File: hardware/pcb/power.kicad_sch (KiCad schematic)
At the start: 49 parts, among them J1 LiPo, J12 Solar, J13 USB-C, U1 AP63205, U11 USBLC6, U12 TP5100, U7 CN3722, U8 MT3608

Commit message: fix(sch): update J1 and L2 footprints in power.kicad_sch
J1 was still referencing the old Connector_JST:JST_XH_B2B-XH-AM footprint
after the switch to XT30PW-F. L2 was still referencing L_2512_6332Metric
after the footprint correction to L_Vishay_IFSC-1515AH_4x4x1.8mm.
Both caused errors in KiCad netlist import.

Co-Authored-By: Claude Sonnet 4.6 <noreply@anthropic.com>
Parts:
- J1: footprint Connector_JST:JST_XH_B2B-XH-AM_1x02_P2.50mm_Horizontal -> WellD:XT30PW-F_RightAngle
- L2: footprint Inductor_SMD:L_2512_6332Metric -> Inductor_SMD:L_Vishay_IFSC-1515AH_4x4x1.8mm
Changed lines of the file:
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@@
 			)
 		)
-		(property "Footprint" "Connector_JST:JST_XH_B2B-XH-AM_1x02_P2.50mm_Horizontal"
+		(property "Footprint" "WellD:XT30PW-F_RightAngle"
 			(at 0 0 0)
 			(hide yes)
@@
 			)
 		)
-		(property "Footprint" "Inductor_SMD:L_2512_6332Metric"
-			(at 0 0 0)
-			(hide yes)
+		(property "Footprint" "Inductor_SMD:L_Vishay_IFSC-1515AH_4x4x1.8mm"
+			(at 0 0 0)
+			(hide yes)

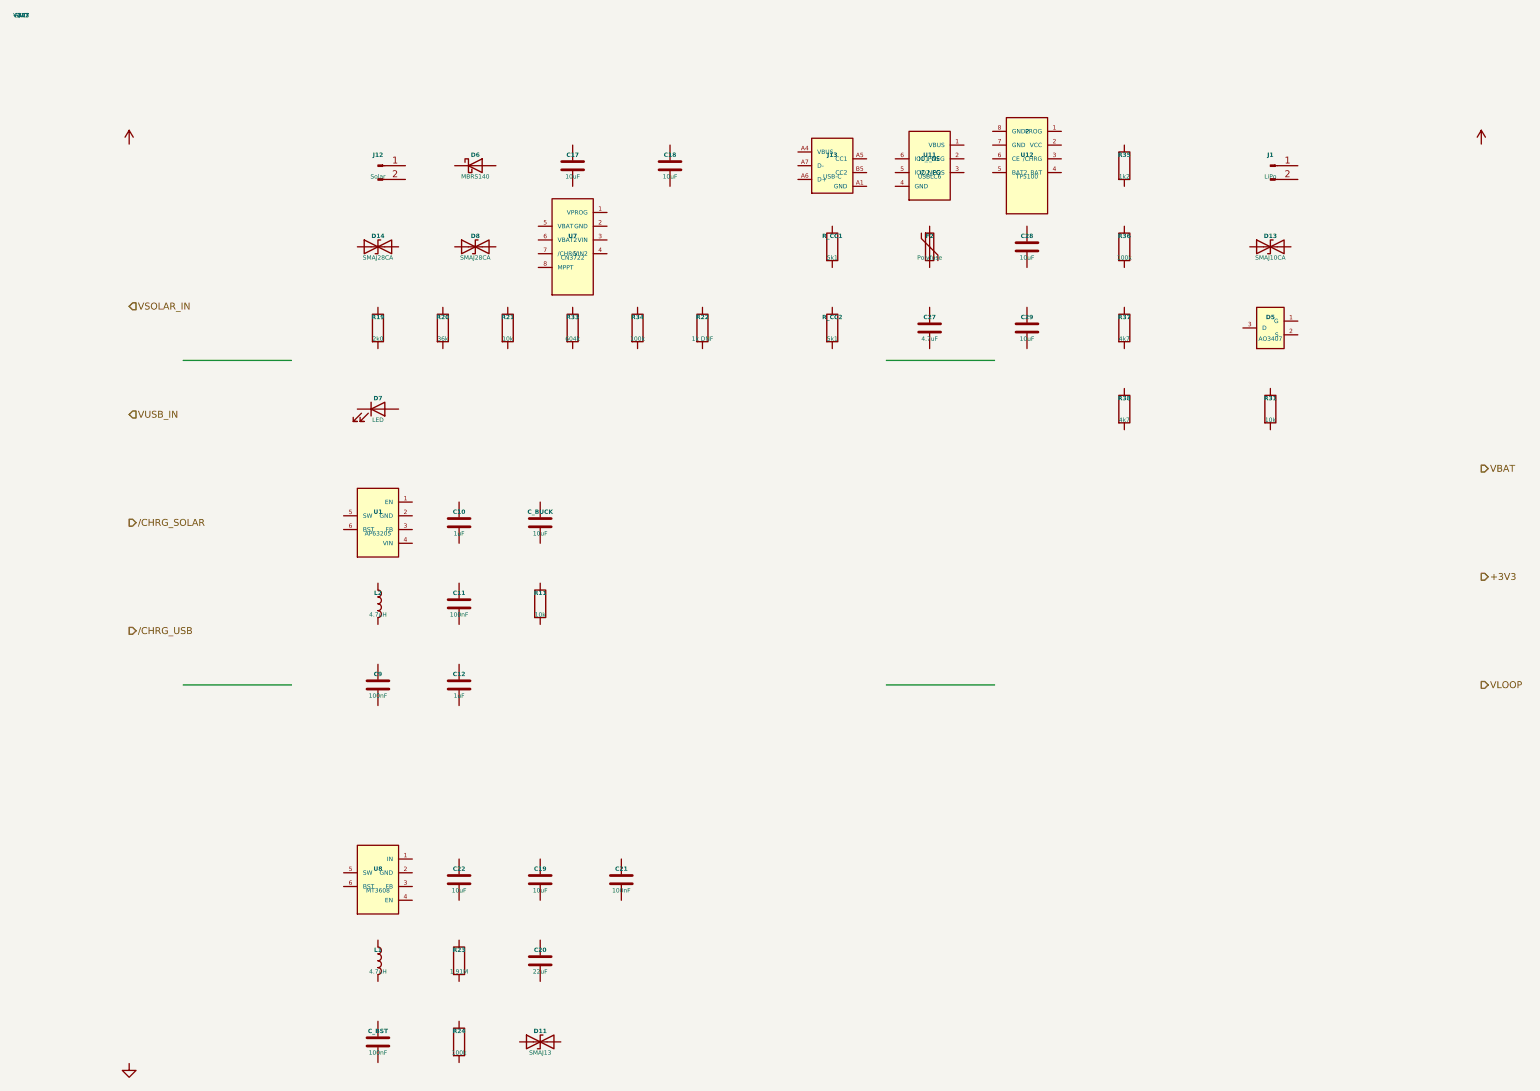
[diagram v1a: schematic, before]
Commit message: hw(pcb): fix J1 XT30 placement — rotation 270°, correct pad names/drill
The community AMASS_XT30PW-M footprint has pads at y=10mm (10mm from
the connector face) and 5mm pin pitch. To mount at the left wall with
the mating face pointing outward, J1 needs rotation 270°, not 180°.

- Footprint: rename pads P→1, N→2 to match schematic pin numbers;
  drill 1.7→1.8mm (our IPC-2221 spec)
- generate_kicad.py: J1 board pos (5.6,33.5)→(2.0,33.5), rot 180→270;
  update courtyard keepout comment
- Regenerate welld.kicad_pcb: J1 now at PCB (67,80) @270°

At 270° from board (2,33.5): mating face at board x≈-1mm (accessible
through left-wall case cutout), power pins at board (12,31)+(12,36),
courtyard X -1.2..13.5, Y 26.6..40.4. Case cutout Y unchanged.

Co-Authored-By: Claude Sonnet 4.6 <noreply@anthropic.com>
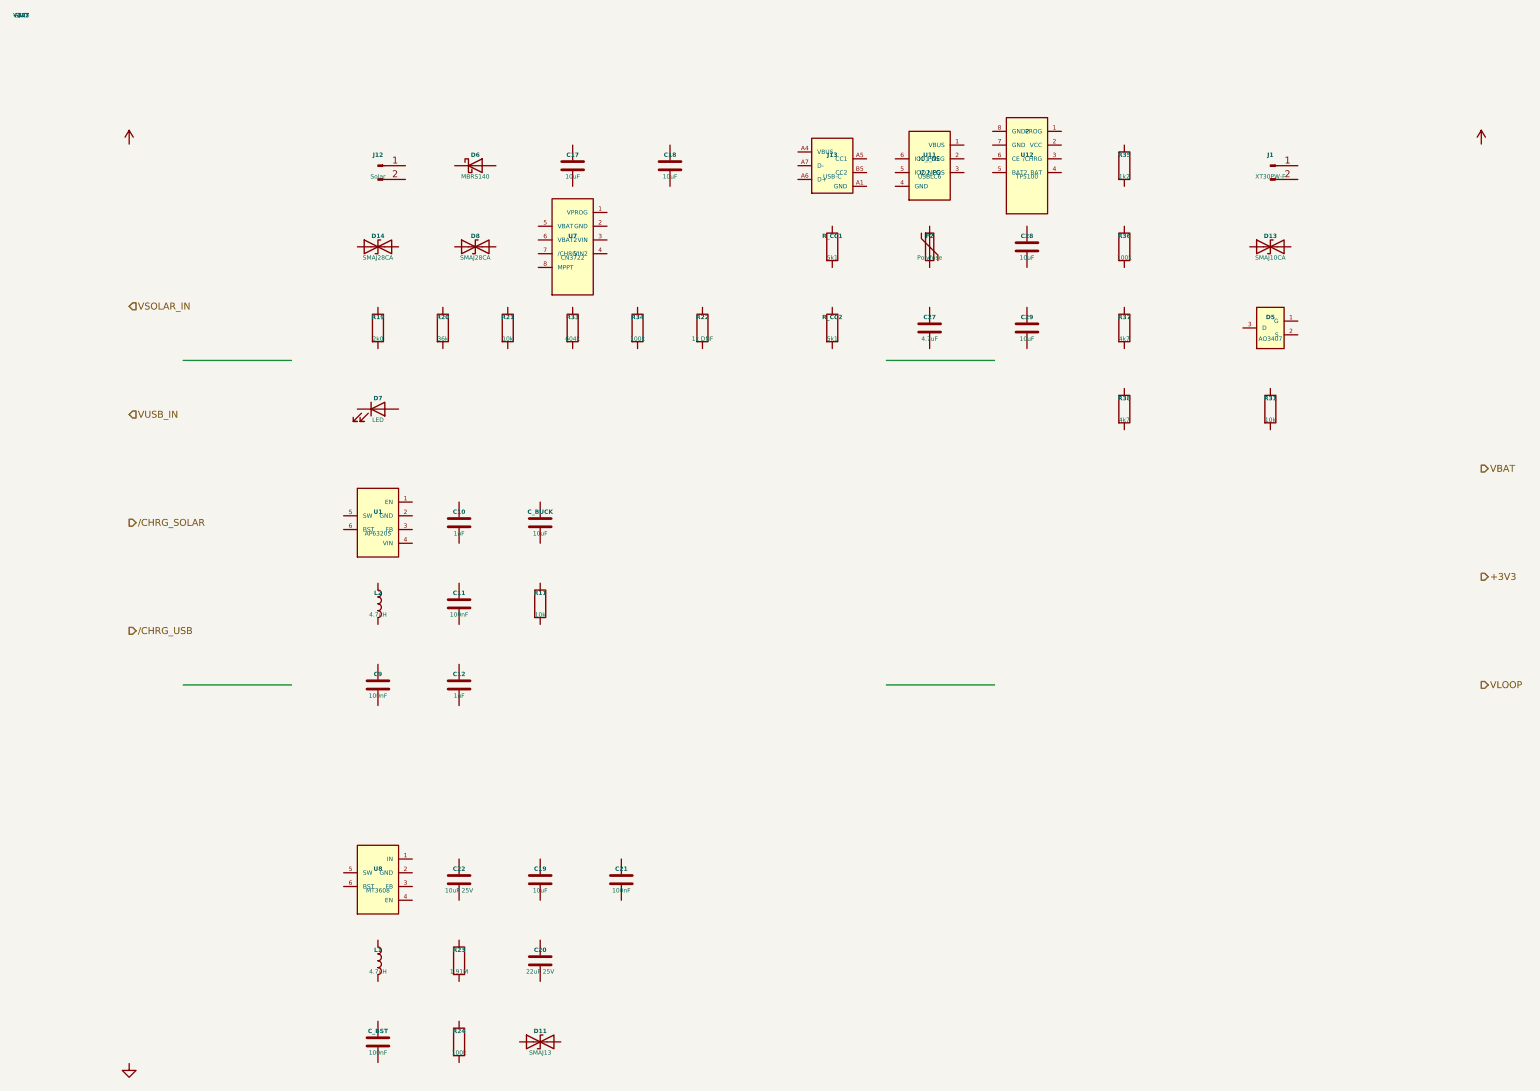
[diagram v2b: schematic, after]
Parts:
- C20: value 22uF -> 22uF 25V
- C22: value 10uF -> 10uF 25V
- J1: value LiPo -> XT30PW-F; LCSC C457925 -> C601498

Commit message: fix(sch): eliminate all structural ERC violations in hierarchical schematic
Three root causes fixed in generate_kicad.py:

1. Left-side sheet pins used angle=0 — kicad-cli upgrade snapped them to
   the right border, colliding with right-side pins and causing
   multiple_net_names and unconnected_wire_endpoint. Fixed: px==0 pins
   now use angle=180 (outward-left), px>0 pins keep angle=0.

2. Subsheet hierarchical labels and power symbols were at off-grid
   positions (20 mm, 50 mm, 70 mm, …). Replaced with 1.27 mm-aligned
   values (25.4, 50.8, 63.5, … multiples of 500 mil).

3. _remap_positions() produced arbitrary floats. Added _snap() that
   rounds every remapped coordinate to the nearest 1.27 mm grid point,
   eliminating component-pin endpoint_off_grid violations.

Also: paper size bumped A3 → A2 (layout reaches y ≈ 407 mm, exceeding
A3 height of 297 mm). SHEETS definition pinned to 1.27 mm-aligned
origins and heights; MCU left-side pins reordered to match power
right-side y-levels for direct horizontal wires.

ERC result: 588 → 404 violations.
Eliminated: endpoint_off_grid (−129), unconnected_wire_endpoint (−4),
wire_dangling (−2), multiple_net_names (−1).
Remaining 404 are structural (pin_not_connected, label_dangling) that
require full intra-sheet wiring — not addressable by the generator alone.

Netlist unchanged: 118 refs, 34 nets.

Co-Authored-By: Claude Sonnet 4.6 <noreply@anthropic.com>
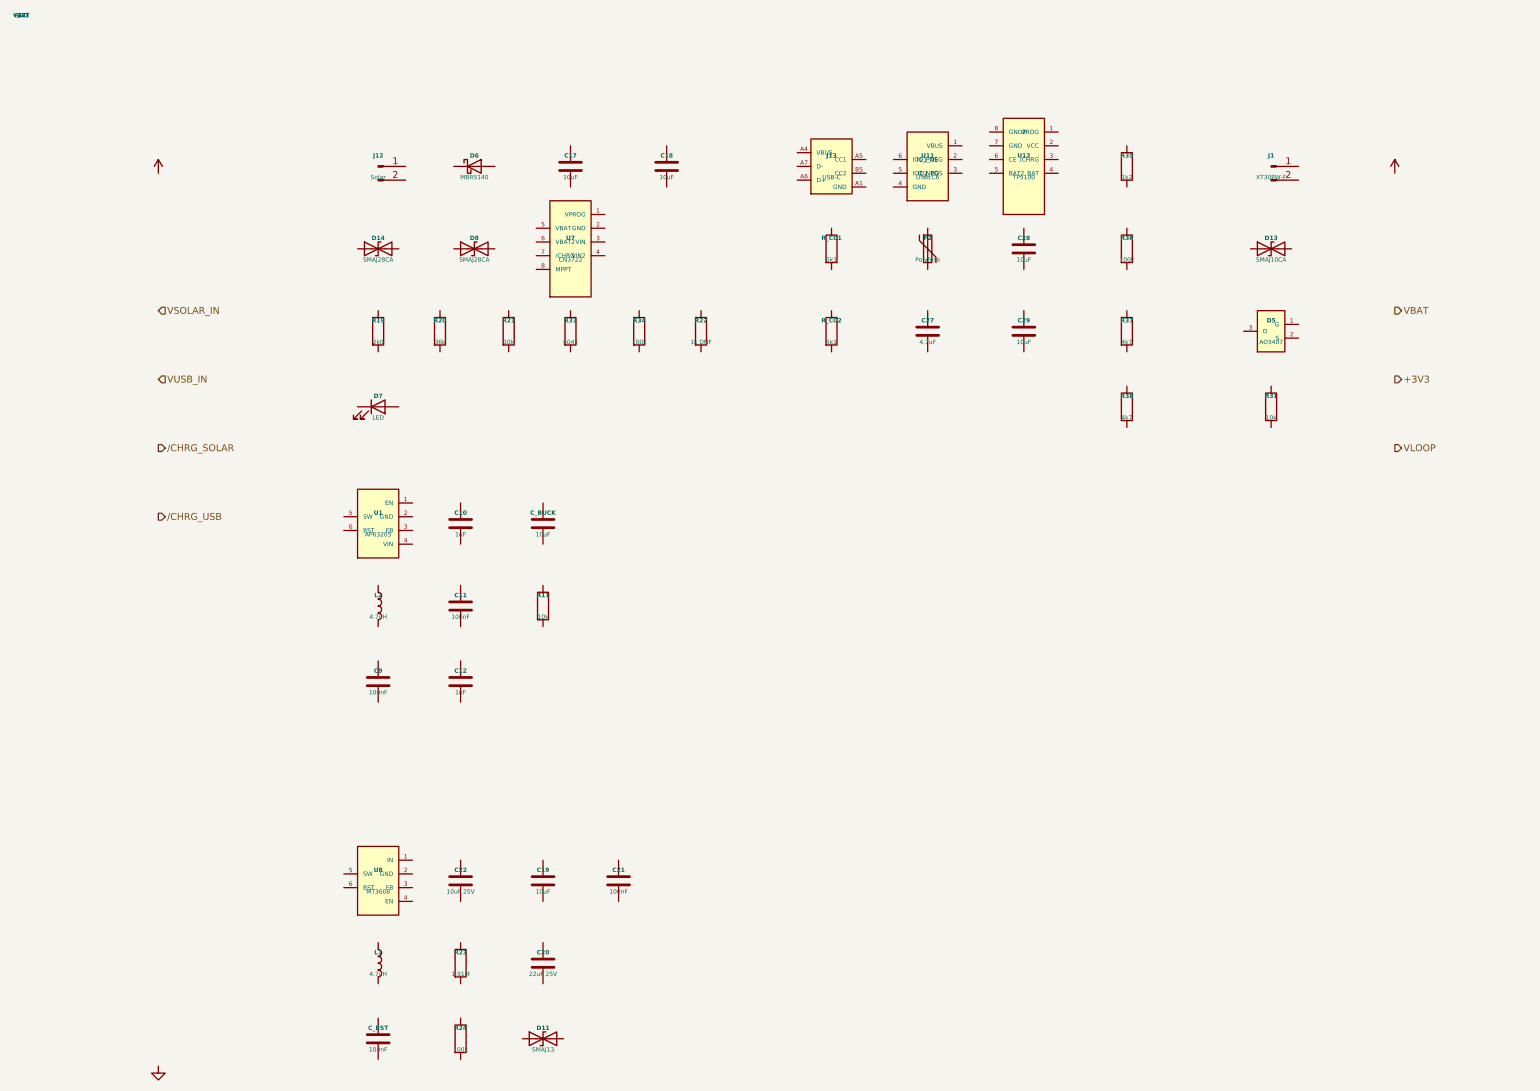
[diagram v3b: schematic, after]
